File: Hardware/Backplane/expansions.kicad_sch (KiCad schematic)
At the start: 8 parts, among them U102 TCA9548APWR, U2901 P2X8C4M64P, U3001 NL17SZS11DFT2G-Q, U3002 NL17SZS11DFT2G-Q

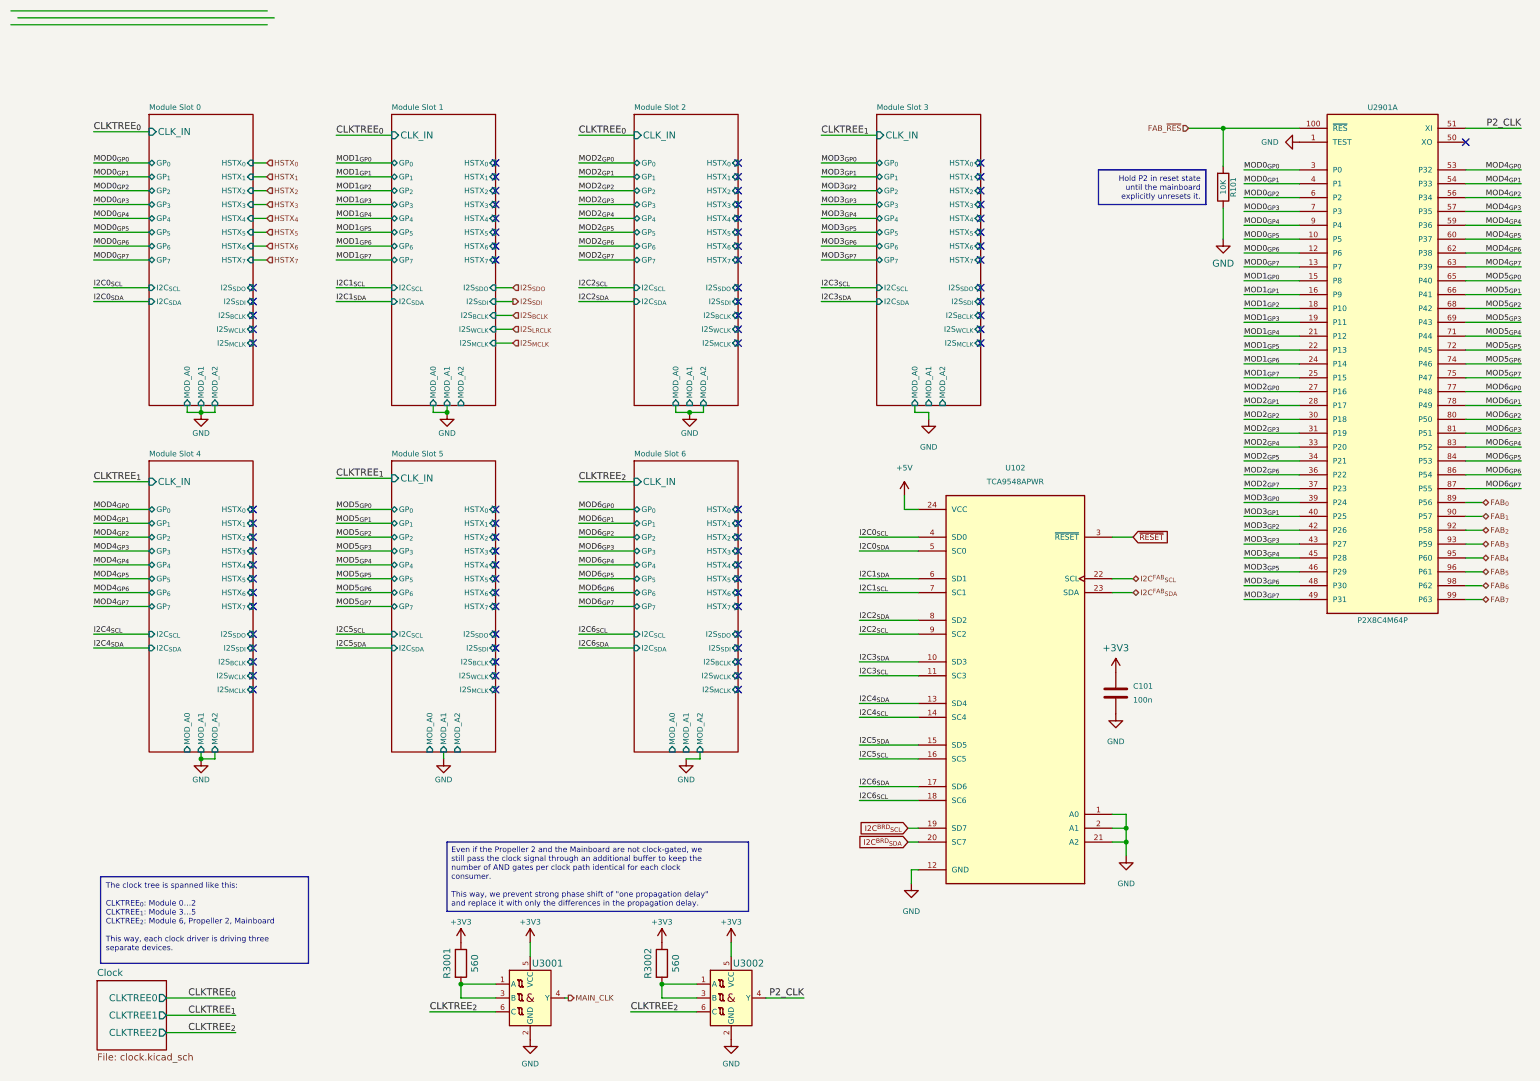
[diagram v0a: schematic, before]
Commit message: Fixes two issues regarding the power supply of the TCA9548APWR, routes TCA9548APWR.RESET to the main board controller.
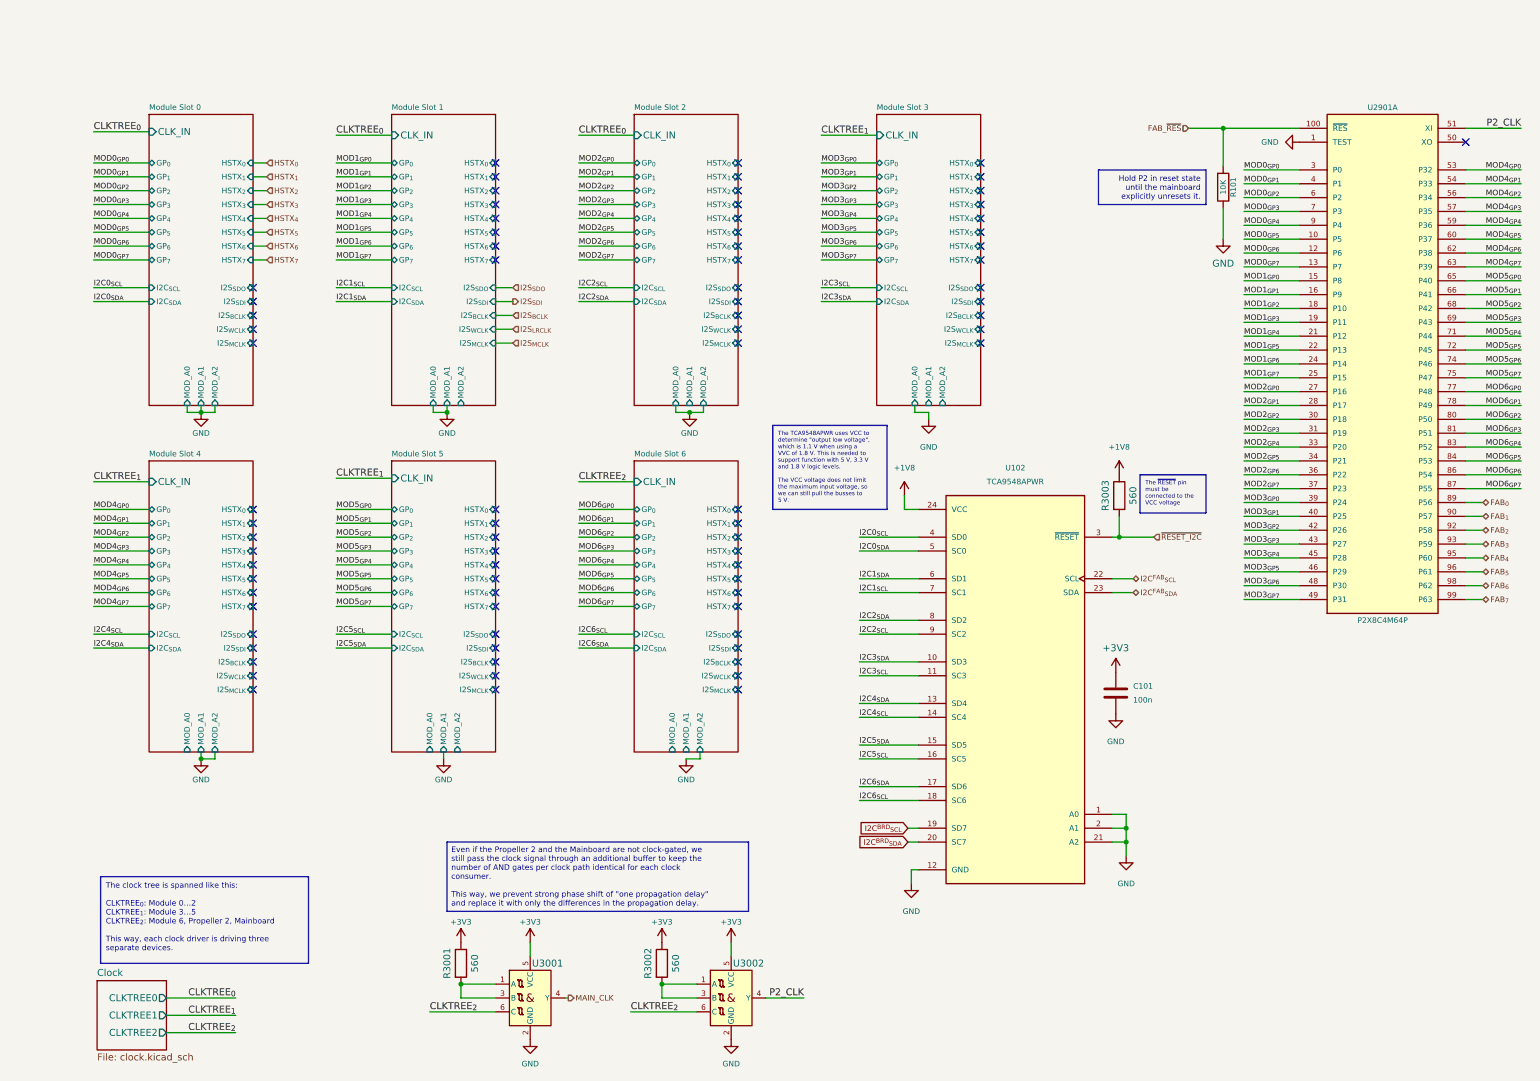
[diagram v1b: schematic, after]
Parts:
- added R3003: 560, Resistor_SMD:R_0603_1608Metric, symbol Device:R
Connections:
- net +5V renamed +1V8
- net +1V8: now also R3003.1
- net ~{RESET} renamed ~{RESET_I2C}
- net ~{RESET_I2C}: now also R3003.2

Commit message: Fixes several issues with the backplane schematic.
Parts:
- added R1114: 10K, Resistor_SMD:R_0603_1608Metric, symbol Device:R
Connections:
- net +1V8: now also C101.2, R1114.1
- net +3V3: no longer C101.2
- net GND: no longer U102.1 (A0), U102.2 (A1), U102.21 (A2)
- net I2C0_{SCL}: now also U102.5 (SC0); no longer U102.4 (SD0)
- net I2C0_{SDA}: now also U102.4 (SD0); no longer U102.5 (SC0)
- net I2C^{BRD}_{SCL}: now also U102.20 (SC7); no longer U102.19 (SD7)
- net I2C^{BRD}_{SDA}: now also U102.19 (SD7); no longer U102.20 (SC7)
- net ~{RESET_I2C}: now also R1114.2; no longer R3003.2
- new net: R3003.2, U102.1 (A0), U102.2 (A1), U102.21 (A2)
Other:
- moved on the sheet: C101

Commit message: Improves backplane schematic even more
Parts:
- removed R3001, R3002: 560, Resistor_SMD:R_0603_1608Metric, symbol Device:R
- removed U3001, U3002: NL17SZS11DFT2G-Q, Package_TO_SOT_SMD:SOT-363_SC-70-6, symbol Home Computer:NL17SZS11DFT2G-Q
- added C217, C218: 100n, Capacitor_SMD:C_0603_1608Metric, symbol Device:C
- added R207, R208: 560, Resistor_SMD:R_0603_1608Metric, symbol Device:R
- added U46, U47: NL7SZ57DBVT1G, Package_TO_SOT_SMD:SC-74-6_1.55x2.9mm_P0.95mm, symbol Home Computer:NL7SZ57DBVT1G
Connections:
- net +3V3: now also C217.2, C218.2, R207.2, R208.2, U46.5 (VCC), U47.5 (VCC)
- net CLKTREE_{2}: now also U46.1 (B), U47.1 (B)
- net GND: now also C217.1, C218.1, U46.2 (GND), U46.3 (A), U47.2 (GND), U47.3 (A)
- net MAIN_CLK: now also U46.4 (Y)
- net P2_CLK: now also U47.4 (Y)
- new net: R207.1, U46.6 (C)
- new net: R208.1, U47.6 (C)
- no-connect marks 79 -> 88
